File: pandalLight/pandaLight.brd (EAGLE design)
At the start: 83 x 57.4 mm, 126 parts, among them J1 PJ-037A, U1 MIC2230-XXYML, U10 TPD12S016PWR, U11 PAN1322, U2 6SLX9TQG144, U3 93LC46BT-I/OT, U4 FT2232HL, U5 TPD12S016PWR, U6 20Mhz, U7 TXB0104RGYR, U8 TPD12S016PWR, U9 M25P40-VMN, X1 USBUB-S, X2 HDMI_RECEPTICAL_A, X3 HDMI_RECEPTICAL_A, X4 HDMI_RECEPTICAL_A, X5 PMOD-2X6, X6 PMOD-2X6, Y1 403

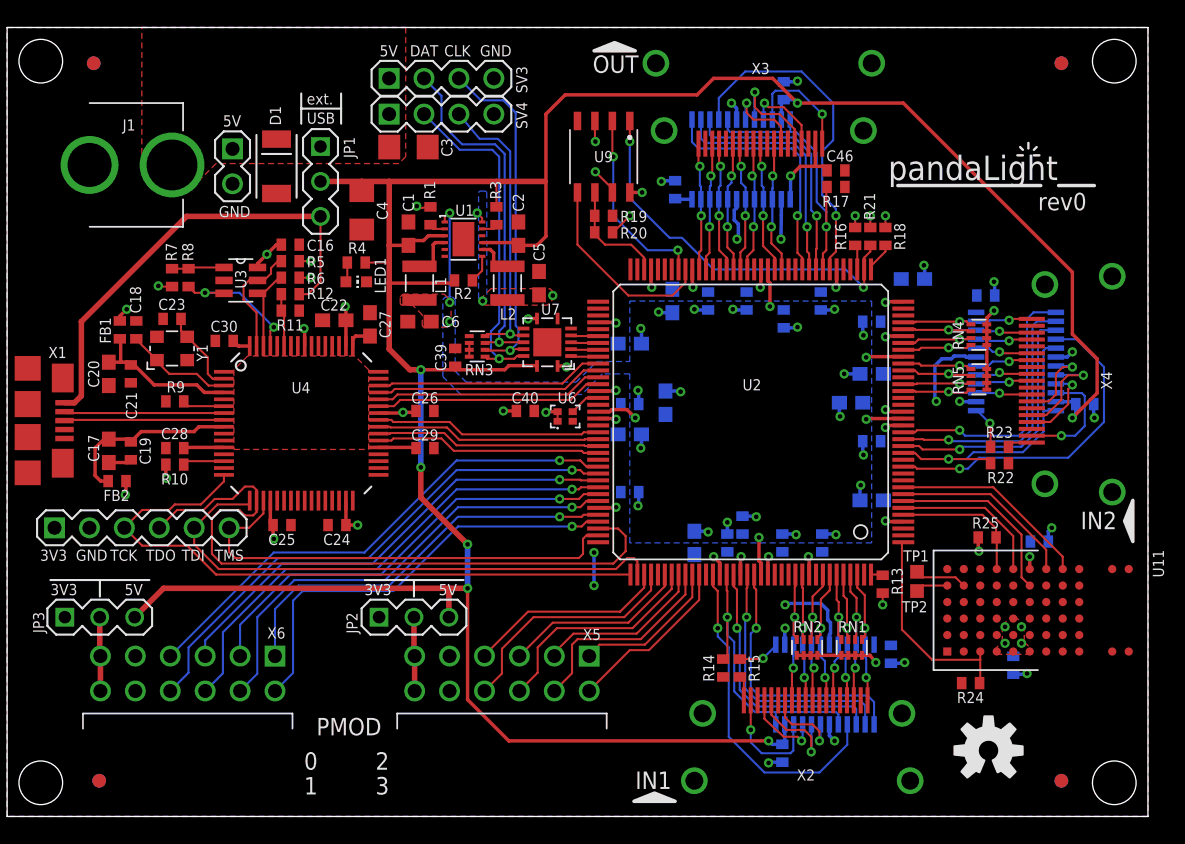
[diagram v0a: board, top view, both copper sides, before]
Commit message: Corrected wrong BOMex part number of the inductors (after ordering them...); Switched to smaller 0402, 0603, 1206 footprint: Many of my hand placed passives are crooked; Moved all names away from vias
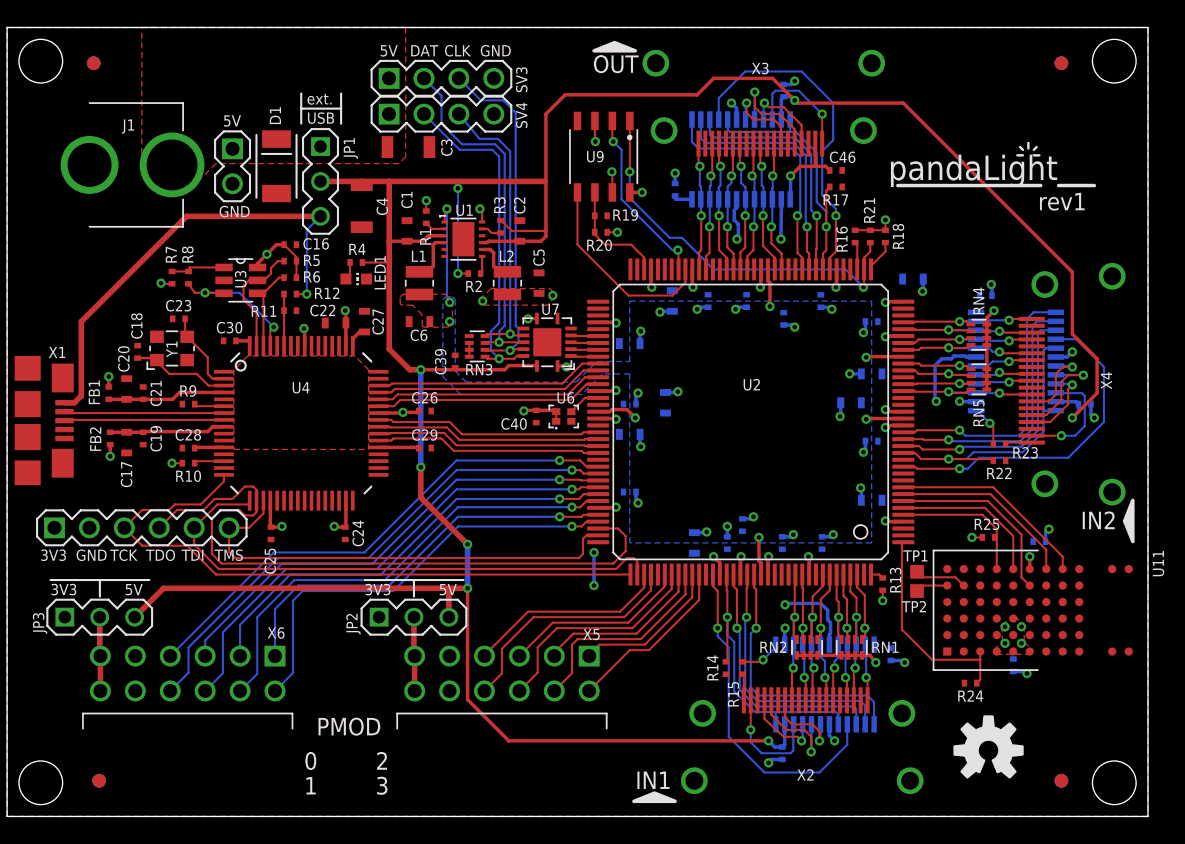
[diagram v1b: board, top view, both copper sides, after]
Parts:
- L1, L2: device pandaLight:1008 -> pandaLight:VLS-E_1008
- moved FB1 4.67 mm to (7.40, 30.8)
- moved FB2 3.14 mm to (7.50, 27.5), turned to 90 degrees
- moved C20 1.70 mm to (8.70, 31.1), turned to 90 degrees
- moved C21 1.66 mm to (9.90, 30.8), turned to 90 degrees
- moved C18 1.60 mm to (9.50, 33.8)
- moved C17 1.43 mm to (8.70, 27.2)
- moved C19 1.27 mm to (9.90, 27.5)
- moved R9 1.02 mm to (13.2, 30.0)
- moved R10 1.00 mm to (13.2, 25.7)
- moved C28 1.00 mm to (13.2, 26.8)
- moved C25 1.00 mm to (19.2, 20.6), turned to 270 degrees
- moved R2 0.94 mm to (34.0, 39.5)
- moved C40 0.89 mm to (38.5, 29.1), turned to 270 degrees
- moved R3 0.85 mm to (35.9, 42.9)
- moved C24 0.85 mm to (24.6, 20.6), turned to 270 degrees
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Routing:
- net GND: track 59.5 -> 54.4 mm
- net N$31: track 13.3 -> 8.44 mm
- net +5V: track 208.6 -> 213.2 mm, vias 7 -> 9
- net N$28: track 11.0 -> 8.58 mm
- net N$43: track 14.1 -> 13.1 mm
- net N$11: track 3.07 -> 2.19 mm
- net +1V8: track 8.90 -> 8.05 mm
- net N$13: track 3.03 -> 2.19 mm
- net N$4: track 2.04 -> 1.30 mm
- net N$5: track 8.01 -> 7.30 mm
- net +1V2: track 21.3 -> 21.9 mm
- net +3V3: track 74.1 -> 73.5 mm, vias 53 -> 48
- net USB_VBUS: track 34.1 -> 34.2 mm, vias 0 -> 1
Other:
- board text added: "rev1"
- board text removed: "rev0"

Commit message: Trying EagleUp; Now using R* and C* parts for caps and resistors
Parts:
- C1, C10, C11, C17, C2, C20, C22, C27, C31, C36, C41, C47, C5, C6, C7, C8, C9: device pandaLight:0603 -> pandaLight:C0603
- C12, C13, C14, C15, C16, C18, C19, C21, C23, C24, C25, C26, C28, C29, C30, C32, C33, C34, C35, C37, C38, C39, C40, C42, C43, C44, C45, C46, C48, C49, C50, C51, C52, C53: device pandaLight:0402 -> pandaLight:C0402
- C3, C4: device pandaLight:1206 -> pandaLight:C1206
- FB1, FB2, R1, R10, R11, R12, R13, R14, R15, R16, R17, R18, R19, R2, R20, R21, R22, R23, R24, R25, R3, R4, R5, R6, R7, R8, R9: device pandaLight:0402 -> pandaLight:R0402

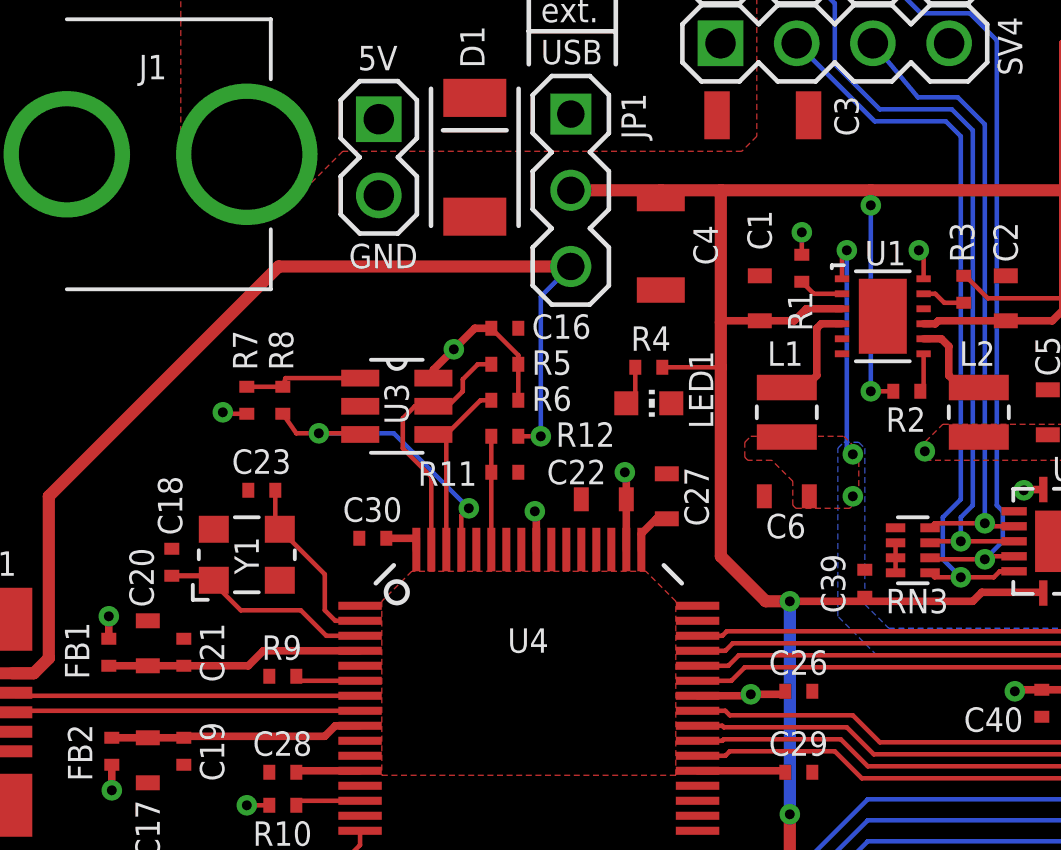
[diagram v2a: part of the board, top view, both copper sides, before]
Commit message: First draft of SketchUp model; Set extra part for ferrite beads
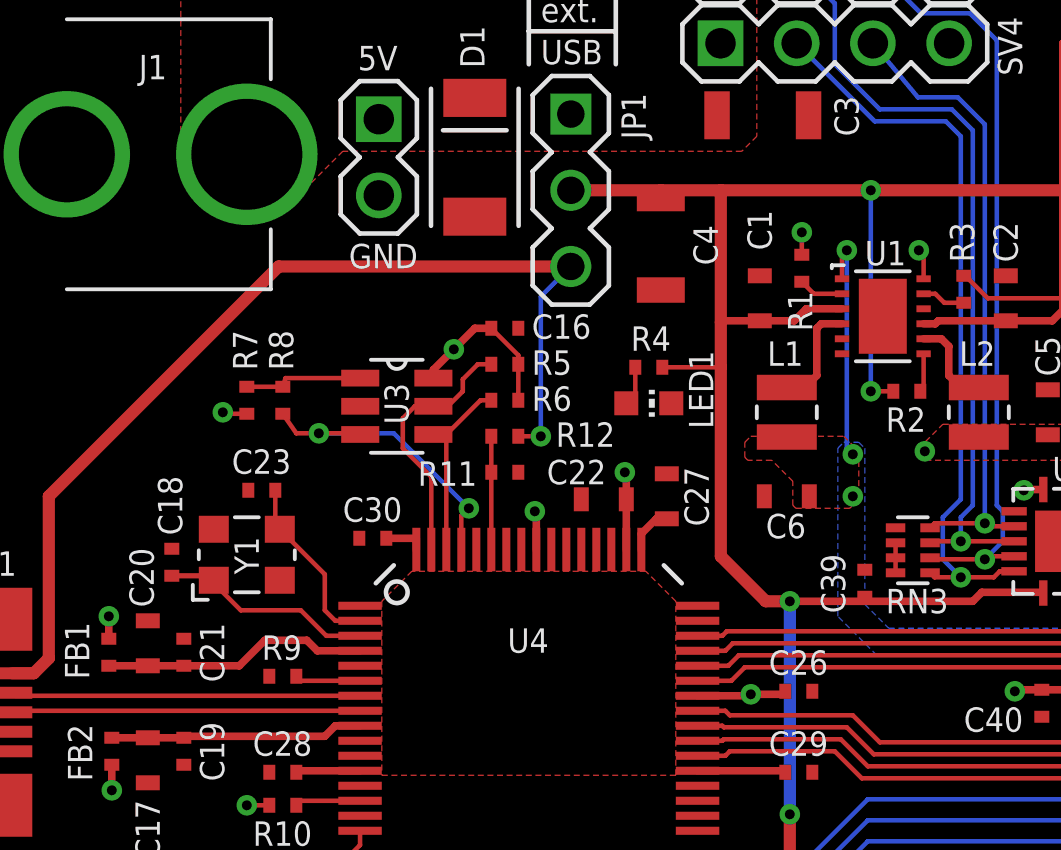
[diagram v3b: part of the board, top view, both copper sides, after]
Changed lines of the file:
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@@
 <wire x1="53.8" y1="37.05" x2="53.15" y2="37.05" width="0.254" layer="16"/>
 <wire x1="53.15" y1="37.05" x2="53" y2="36.9" width="0.254" layer="16"/>
-<wire x1="15.775" y1="30.35" x2="15.775" y2="32.35" width="0" layer="19" extent="1-1"/>
 </signal>
 <signal name="+3V3" class="1">
@@
 <wire x1="33.55" y1="39.5" x2="32.8" y2="39.5" width="0.1524" layer="1"/>
 <via x="32.8" y="39.5" extent="1-16" drill="0.3302"/>
-<wire x1="32.8" y1="39.5" x2="32.8" y2="45.7" width="0.1524" layer="16"/>
 <wire x1="32.6" y1="32.65" x2="32.6" y2="32.6" width="0.254" layer="1"/>
 <wire x1="32.6" y1="32.6" x2="32.7" y2="32.5" width="0.254" layer="1"/>
@@
 <wire x1="56.325" y1="52.175" x2="56.5" y2="52.35" width="0.254" layer="16"/>
 <wire x1="25.8" y1="45.925" x2="25.8" y2="46.2" width="0.4064" layer="1"/>
-<via x="32.8" y="45.7" extent="1-16" drill="0.3302"/>
-<wire x1="32.8" y1="45.7" x2="32.8" y2="46.2" width="0.1524" layer="1"/>
+<wire x1="32.8" y1="39.5" x2="32.8" y2="46.2" width="0.1524" layer="16"/>
+<via x="32.8" y="46.2" extent="1-16" drill="0.3302"/>
 </signal>
 <signal name="N$27">
@@
 <contactref element="C21" pad="1"/>
 <contactref element="C20" pad="1"/>
-<wire x1="9.9" y1="30.35" x2="12.05" y2="30.35" width="0.254" layer="1"/>
-<wire x1="12.05" y1="30.35" x2="12.55" y2="30.85" width="0.254" layer="1"/>
-<wire x1="15.775" y1="30.85" x2="12.55" y2="30.85" width="0.254" layer="1"/>
+<wire x1="9.9" y1="30.35" x2="11.75" y2="30.35" width="0.254" layer="1"/>
+<wire x1="11.75" y1="30.35" x2="12.6" y2="31.2" width="0.254" layer="1"/>
 <wire x1="9.9" y1="30.35" x2="8.7" y2="30.35" width="0.254" layer="1"/>
 <wire x1="8.7" y1="30.35" x2="7.4" y2="30.35" width="0.254" layer="1"/>
+<wire x1="12.6" y1="31.2" x2="14" y2="31.2" width="0.254" layer="1"/>
+<wire x1="14" y1="31.2" x2="14.35" y2="30.85" width="0.254" layer="1"/>
+<wire x1="15.775" y1="30.85" x2="14.35" y2="30.85" width="0.254" layer="1"/>
 </signal>
 <signal name="N$31">

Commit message: Forgot saving
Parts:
- FB1, FB2: device pandaLight:R0402 -> pandaLight:FB0402
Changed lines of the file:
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@@
 <layer number="220" name="220bmp" color="21" fill="1" visible="no" active="no"/>
 <layer number="221" name="221bmp" color="22" fill="1" visible="no" active="no"/>
+<layer number="222" name="222bmp" color="23" fill="1" visible="no" active="no"/>
 <layer number="223" name="223bmp" color="24" fill="1" visible="no" active="no"/>
 <layer number="224" name="224bmp" color="25" fill="1" visible="no" active="no"/>
@@
 <attribute name="VALUE" x="28.55" y="44.6" size="0.8128" layer="27" ratio="15" rot="R270"/>
 </element>
-<element name="FB2" library="pandaLight" package="R0402" value="1A" x="7.5" y="27.5" smashed="yes" rot="R90">
+<element name="FB2" library="pandaLight" package="FB0402" value="1A" x="7.5" y="27.5" smashed="yes" rot="R90">
 <attribute name="PARTNO" value="BK1005HS100-T" x="124.34" y="74.49" size="1.778" layer="27" rot="R90" display="off"/>
 <attribute name="NAME" x="6.85" y="26.5" size="0.8128" layer="25" ratio="15" rot="R90"/>
 <attribute name="VALUE" x="9.45" y="26.5" size="0.8128" layer="27" ratio="15" rot="R90"/>
 </element>
-<element name="FB1" library="pandaLight" package="R0402" value="1A" x="7.4" y="30.8" smashed="yes" rot="R270">
+<element name="FB1" library="pandaLight" package="FB0402" value="1A" x="7.4" y="30.8" smashed="yes" rot="R270">
 <attribute name="PARTNO" value="BK1005HS100-T" x="-109.44" y="-21.27" size="1.778" layer="27" rot="R270" display="off"/>
 <attribute name="NAME" x="6.75" y="29.9" size="0.8128" layer="25" ratio="15" rot="R90"/>

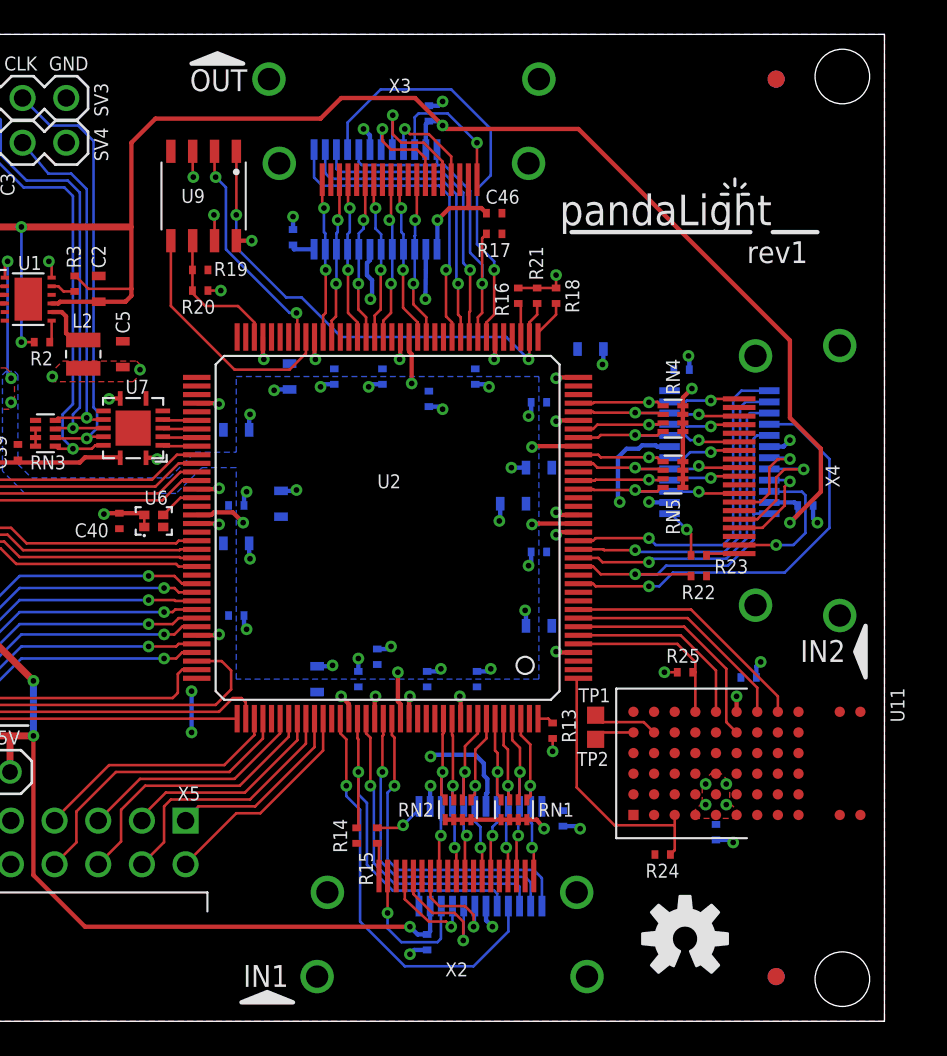
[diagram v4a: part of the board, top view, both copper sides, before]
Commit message: Corrected wrongly aligned HDMI connector; First version of SketchUp render, only the bluetooth module is missing
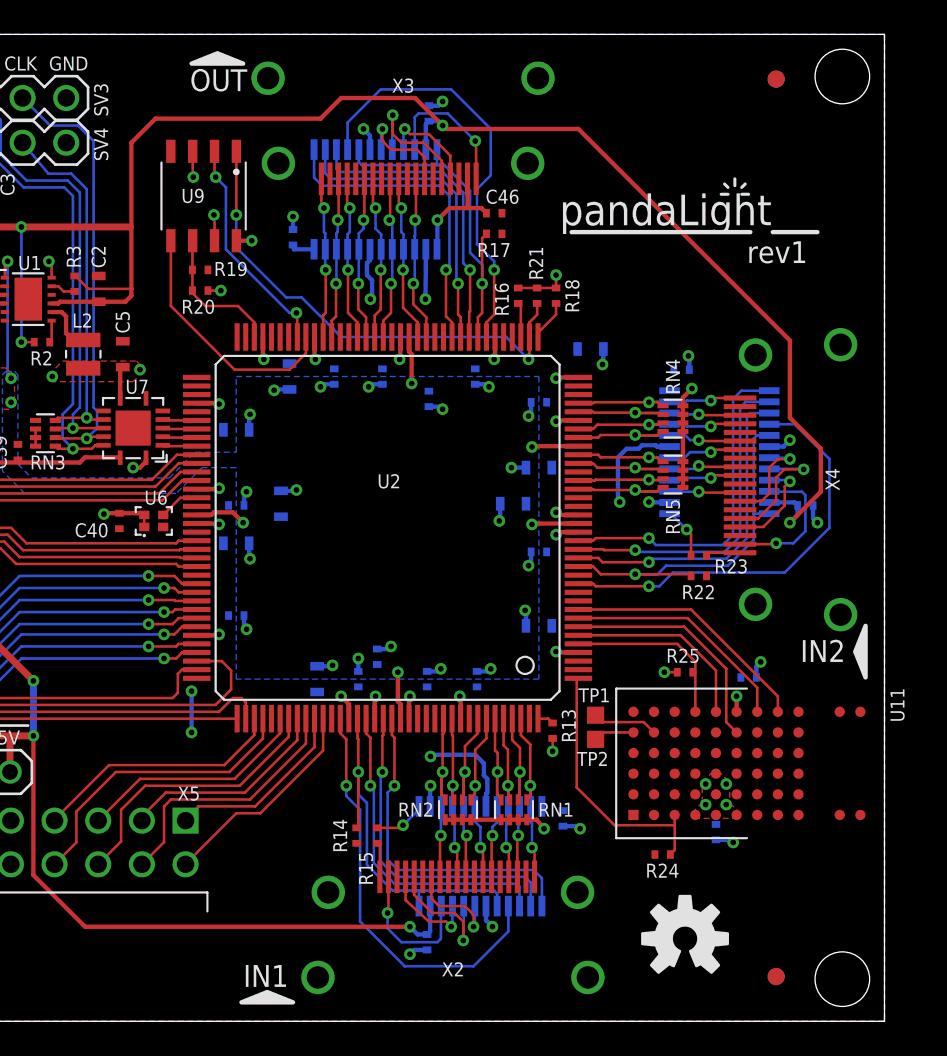
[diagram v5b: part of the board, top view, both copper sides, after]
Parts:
- moved X2 0.20 mm to (57.9, 4.50)
- moved X3 0.20 mm to (55.0, 52.9)
- moved X4 0.20 mm to (78.5, 31.5)
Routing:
- net +3V3: track 73.5 -> 75.2 mm, vias 48 -> 47
